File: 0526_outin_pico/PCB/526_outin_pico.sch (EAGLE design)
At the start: 16 parts

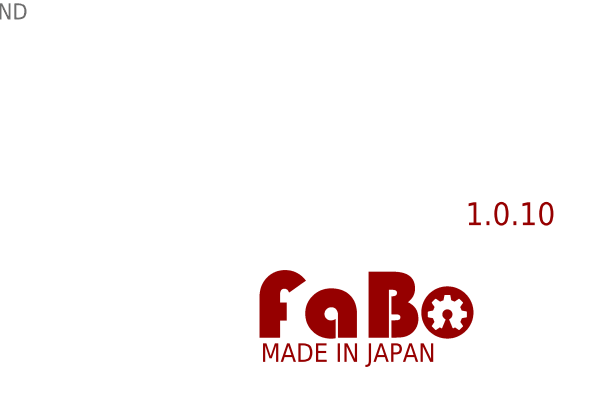
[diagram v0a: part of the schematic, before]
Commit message: #526 outin_pico　ロゴ修正
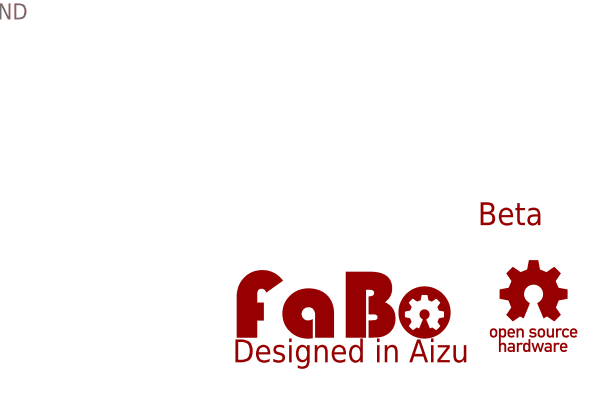
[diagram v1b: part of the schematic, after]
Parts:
- removed U$10: (no value), FaBo-etc:LOGO_FABO-M
- added LOGO1: (no value), component:LOGO_FABO-M
- added U$3: LOGO_OSHW-M_BOTTOM, component:LOGO_OSHW-M_BOTTOM
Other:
- note added: "Beta"
- note removed: "1.0.10"
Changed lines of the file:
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@@
 <?xml version="1.0" encoding="utf-8"?>
 <!DOCTYPE eagle SYSTEM "eagle.dtd">
-<eagle version="9.5.1">
+<eagle version="9.6.2">
 <drawing>
 <settings>
@@
 <setting verticaltext="up"/>
 </settings>
-<grid distance="0.1" unitdist="inch" unit="inch" style="lines" multiple="1" display="no" altdistance="0.01" altunitdist="inch" altunit="inch"/>
+<grid distance="0.1" unitdist="inch" unit="inch" style="lines" multiple="1" display="yes" altdistance="0.01" altunitdist="inch" altunit="inch"/>
 <layers>
 <layer number="1" name="Top" color="4" fill="1" visible="no" active="no"/>
@@
 </classes>
 <parts>
-<part name="U$10" library="FaBo-etc" deviceset="LOGO_FABO" device="-M"/>
 <part name="D3P" library="FaBo-Template" deviceset="FABO_BRICK_3PIN" device="-HEADER"/>
 <part name="D5P" library="FaBo-Template" deviceset="FABO_BRICK_3PIN" device="-HEADER"/>
@@
 <part name="D5" library="FaBo-Template" deviceset="FABO_BRICK_3PIN" device="-B03B-PASK-1"/>
 <part name="I2C_TOP1" library="FaBo-Template" deviceset="FABO_BRICK_I2C" device="-B04B-PASK-1"/>
+<part name="U$3" library="component" deviceset="LOGO_OSHW" device="-M_BOTTOM"/>
+<part name="LOGO1" library="component" deviceset="LOGO_FABO" device="-M"/>
 </parts>
 <sheets>
 <sheet>
 <plain>
-<text x="373.38" y="20.32" size="2.54" layer="94" align="bottom-center">1.0.10</text>
+<text x="373.38" y="20.32" size="2.54" layer="94" align="bottom-center">Beta</text>
 <text x="208.28" y="198.12" size="2.54" layer="97">DIGITAL (3pin Top 2mm pitch)</text>
 <text x="208.28" y="236.22" size="2.54" layer="97">ANALOG (3pin Side 2mm pitch)</text>
@@
 </plain>
 <instances>
-<instance part="U$10" gate="G$1" x="345.44" y="5.08" smashed="yes"/>
 <instance part="D3P" gate="G$1" x="218.44" y="96.52" smashed="yes" rot="R90">
 <attribute name="NAME" x="210.312" y="91.44" size="1.778" layer="95" rot="R90"/>
@@
 <attribute name="NAME" x="243.332" y="43.18" size="1.778" layer="95" rot="R90"/>
 </instance>
+<instance part="U$3" gate="G$1" x="375.92" y="12.7" smashed="yes"/>
+<instance part="LOGO1" gate="G$1" x="342.9" y="5.08" smashed="yes"/>
 </instances>
 <busses>

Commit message: Pico対応ボード
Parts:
- removed U$16: (no value), RaspberryPi_Pico:RPI_PICO-TH
- added D6P1: (no value), FaBo-Template:FABO_BRICK_3PIN-HEADER
- added U$4: (no value), RaspberryPi_Pico:RPI_PICO-SMD
- renumbered A0 to ADC0, A1 to ADC1, A2 to ADC2, D2 to 2, D3 to 3, D4 to 4, D5 to 5
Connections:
- removed net N$1: U$16.AGND
- new net 5V: 2.VCC, 3.VCC, 4.VCC, 5.VCC, ADC0.VCC, ADC1.VCC, ADC2.VCC, D3P.VCC, D5P.VCC, D6P.VCC, D6P1.VCC, I2C_TOP.VCC, I2C_TOP1.VCC, SERIAL_HW.VCC, U$4.ADC_VREF, U$4.VBUS
- new net PWM_14: D3P.I/O, U$4.GP14
- new net PWM_15: D5P.I/O, U$4.GP15
- new net PWM_16: D6P.I/O, U$4.GP16
- new net PWM_17: D6P1.I/O, U$4.GP17
- net 3V3: now also U$4.3V3; no longer 2.VCC, 3.VCC, 4.VCC, 5.VCC, ADC0.VCC, ADC1.VCC, ADC2.VCC, D3P.VCC, D5P.VCC, D6P.VCC, I2C_TOP.VCC, I2C_TOP1.VCC, SERIAL_HW.VCC, U$16.3V3, U$16.3V3_EN, U$16.ADC_VREF
- net A0: now also U$4.GP26_A0; no longer D3P.I/O, U$16.GP26_A0
- net A1: now also U$4.GP27_A1; no longer D5P.I/O, U$16.GP27_A1
- net A2: now also U$4.GP28_A2; no longer D6P.I/O, U$16.GP28_A2
- net D0: now also U$4.GP0; no longer U$16.GP0
- net D1: now also U$4.GP1; no longer U$16.GP1
- net D2: now also U$4.GP2; no longer U$16.GP2
- net D3: now also U$4.GP3; no longer U$16.GP3
- net D4: now also U$4.GP4; no longer U$16.GP4
- net D5: now also U$4.GP5; no longer U$16.GP5
- net GND: now also D6P1.GND, U$4.AGND, U$4.GND; no longer U$16.GND
- net RESET: now also U$4.RUN; no longer U$16.RUN
- net SCL: now also U$4.GP9; no longer U$16.GP9
- net SDA: now also U$4.GP8; no longer U$16.GP8

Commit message: OUT/IN for Raspberry Pi Pico(Rev.Beta1)　追加
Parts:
- removed 2, 3, 4, 5: (no value), FaBo-Template:FABO_BRICK_3PIN-B03B-PASK-1
- removed ADC0, ADC1, ADC2: (no value), FaBo-Template:FABO_BRICK_3PIN-S03B-PASK-2_LONG
- removed D3P, D5P, D6P, D6P1: (no value), FaBo-Template:FABO_BRICK_3PIN-HEADER
- removed I2C_TOP, I2C_TOP1: (no value), FaBo-Template:FABO_BRICK_I2C-B04B-PASK-1
- removed SERIAL_HW: (no value), FaBo-Template:FABO_BRICK_SERIAL-B04B-PASK-1
- removed U$3: LOGO_OSHW-M_BOTTOM, component:LOGO_OSHW-M_BOTTOM
- removed U$4: (no value), RaspberryPi_Pico:RPI_PICO-SMD
- added A0, A1, A2: (no value), FaBo-Template:FABO_BRICK_3PIN-S03B-PASK-2_LONG
- added D2, D3, D4, D5: (no value), FaBo-Template:FABO_BRICK_3PIN-B03B-PASK-1
- added I2C0, I2C1: (no value), FaBo-Template:FABO_BRICK_I2C-B04B-PASK-1
- added JP1: (no value), FaBo-PIN:SMD-JUMPER-2_SHORT
- added LOGO2: (no value), FaBo-Logo:LOGO_FABO-M
- added PWM14, PWM15, PWM16, PWM17: (no value), FaBo-Template:FABO_BRICK_3PIN-HEADER
- added R1, R2: 5K1, FaBo-Resistors:RESISTOR-0603
- added SERIAL: (no value), FaBo-Template:FABO_BRICK_SERIAL-B04B-PASK-1
- added U1: (no value), FaBo-Boards:RASPBERRY_PI_PICO
- LOGO1: device component:LOGO_FABO-M -> FaBo-Logo:LOGO_OSHW-M_BOTTOM
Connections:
- removed net D0: SERIAL_HW.RX, U$4.GP0
- removed net D1: SERIAL_HW.TX, U$4.GP1
- removed net PWM_14: D3P.I/O, U$4.GP14
- removed net PWM_15: D5P.I/O, U$4.GP15
- removed net PWM_16: D6P.I/O, U$4.GP16
- removed net PWM_17: D6P1.I/O, U$4.GP17
- new net AVDD: A0.VCC, A1.VCC, A2.VCC, U1.ADC_VREF
- new net N$3: JP1.2, R1.2, R2.2
- new net PWM14: PWM14.I/O, U1.GP14
- new net PWM15: PWM15.I/O, U1.GP15
- new net PWM16: PWM16.I/O, U1.GP16
- new net PWM17: PWM17.I/O, U1.GP17
- new net RX: SERIAL.RX, U1.GP1
- new net TX: SERIAL.TX, U1.GP0
- net 3V3: now also JP1.1, U1.3V3; no longer U$4.3V3
- net 5V: now also D2.VCC, D3.VCC, D4.VCC, D5.VCC, I2C0.VCC, I2C1.VCC, PWM14.VCC, PWM15.VCC, PWM16.VCC, PWM17.VCC, SERIAL.VCC, U1.VBUS; no longer 2.VCC, 3.VCC, 4.VCC, 5.VCC, ADC0.VCC, ADC1.VCC, ADC2.VCC, D3P.VCC, D5P.VCC, D6P.VCC, D6P1.VCC, I2C_TOP.VCC, I2C_TOP1.VCC, SERIAL_HW.VCC, U$4.ADC_VREF, U$4.VBUS
- net A0: now also A0.I/O, U1.GP26; no longer ADC0.I/O, U$4.GP26_A0
- net A1: now also A1.I/O, U1.GP27; no longer ADC1.I/O, U$4.GP27_A1
- net A2: now also A2.I/O, U1.GP28; no longer ADC2.I/O, U$4.GP28_A2
- net D2: now also D2.I/O, U1.GP2; no longer 2.I/O, U$4.GP2
- net D3: now also D3.I/O, U1.GP3; no longer 3.I/O, U$4.GP3
- net D4: now also D4.I/O, U1.GP4; no longer 4.I/O, U$4.GP4
- net D5: now also D5.I/O, U1.GP5; no longer 5.I/O, U$4.GP5
- net GND: now also A0.GND, A1.GND, A2.GND, D2.GND, D3.GND, D4.GND, D5.GND, I2C0.GND, I2C1.GND, PWM14.GND, PWM15.GND, PWM16.GND, PWM17.GND, S1.4, SERIAL.GND, U1.AGND@33, U1.GND@13, U1.GND@18, U1.GND@23, U1.GND@28, U1.GND@3, U1.GND@38, U1.GND@8, U1.GND@D2; no longer 2.GND, 3.GND, 4.GND, 5.GND, ADC0.GND, ADC1.GND, ADC2.GND, D3P.GND, D5P.GND, D6P.GND, D6P1.GND, I2C_TOP.GND, I2C_TOP1.GND, SERIAL_HW.GND, U$4.AGND, U$4.GND
- net RESET: now also S1.1, U1.RUN; no longer U$4.RUN
- net SCL: now also I2C0.SCL, I2C1.SCL, R1.1, U1.GP9; no longer I2C_TOP.SCL, I2C_TOP1.SCL, U$4.GP9
- net SDA: now also I2C0.SDA, I2C1.SDA, R2.1, U1.GP8; no longer I2C_TOP.SDA, I2C_TOP1.SDA, U$4.GP8
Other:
- note added: "Beta1"
- note added: "I2C Pull Up"
- note added: "Serial (4pin 2mm pitch)"
- note removed: "Beta"
- note removed: "Serial (4pin 2mm pitch) Hard/Soft"
- moved on the sheet: S1

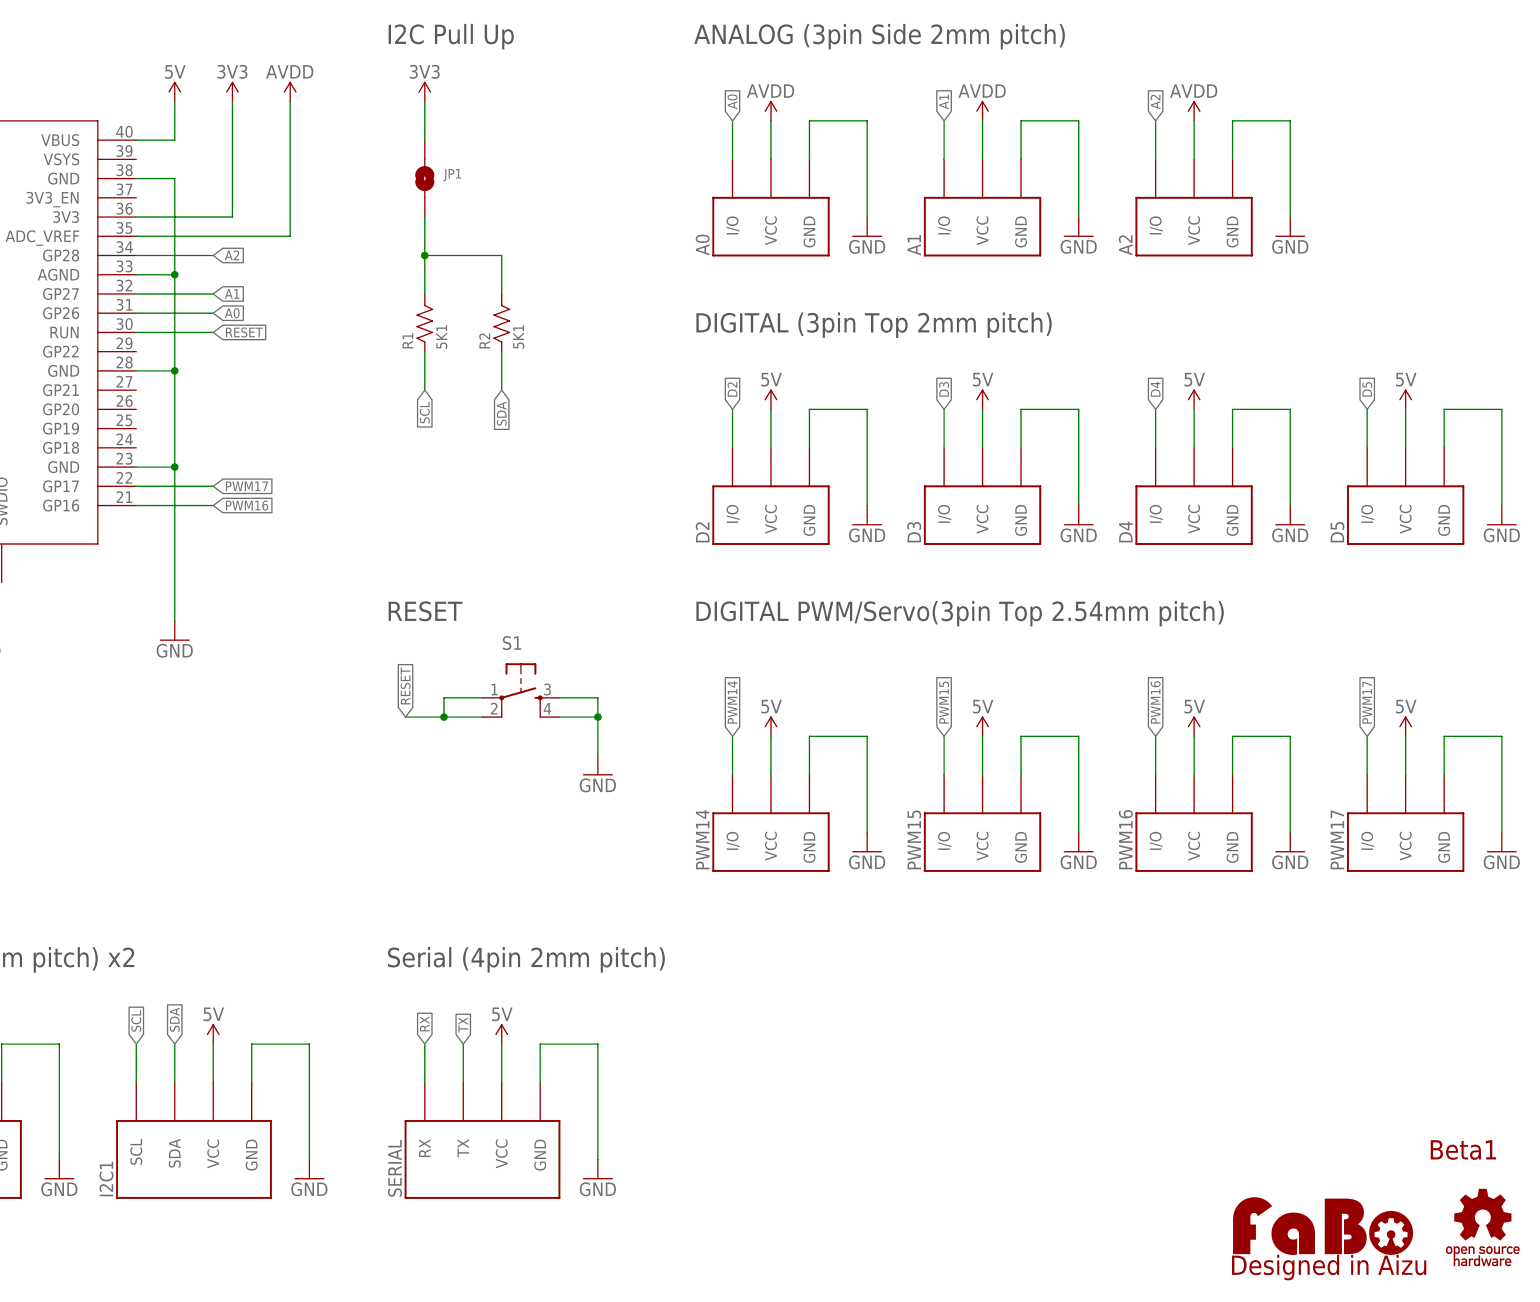
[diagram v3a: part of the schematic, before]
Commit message: アナログ用電源ピンを変更
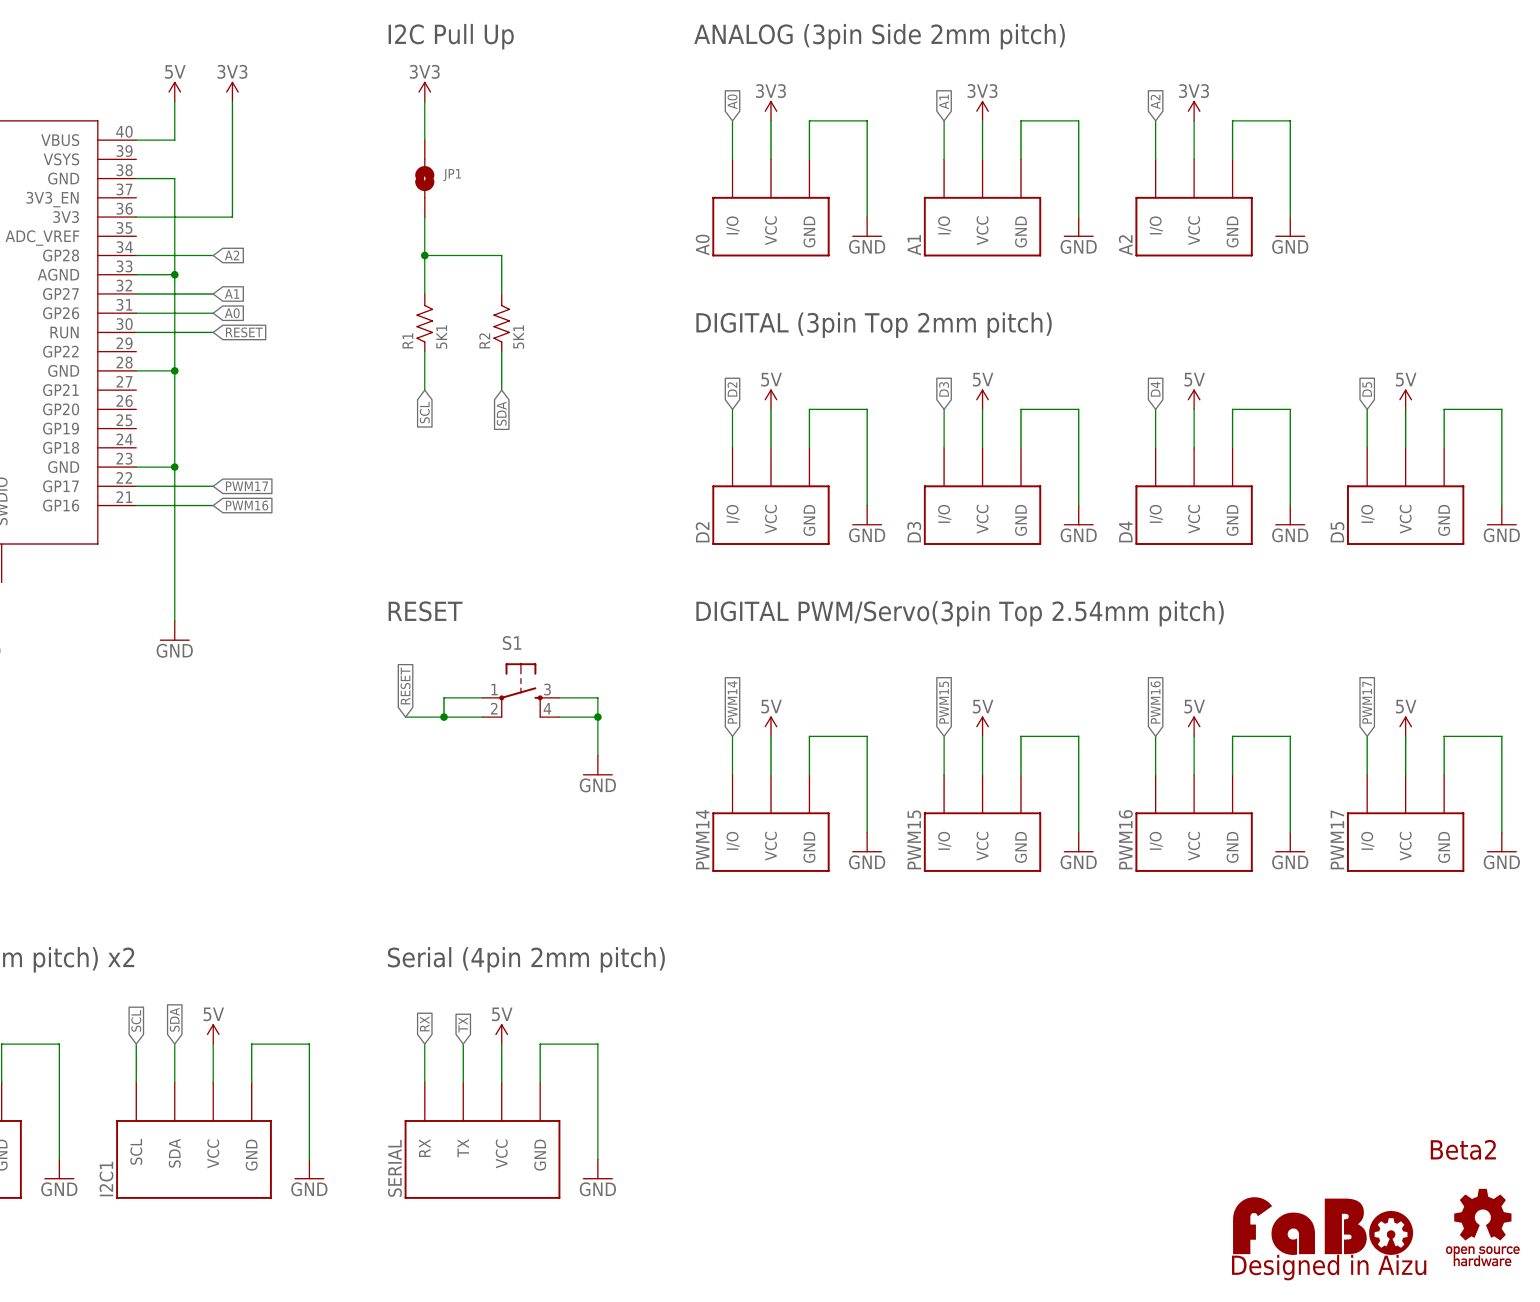
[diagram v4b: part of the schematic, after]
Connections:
- removed net AVDD: A0.VCC, A1.VCC, A2.VCC, U1.ADC_VREF
- net 3V3: now also A0.VCC, A1.VCC, A2.VCC
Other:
- note added: "Beta2"
- note removed: "Beta1"
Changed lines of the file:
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@@
 <part name="U1" library="FaBo-Boards" deviceset="RASPBERRY_PI_PICO" device=""/>
 <part name="5V1" library="FaBo-Symbol" deviceset="5V" device=""/>
-<part name="AVDD1" library="FaBo-Symbol" deviceset="AVDD" device=""/>
 <part name="GND8" library="FaBo-Symbol" deviceset="GND" device=""/>
 <part name="GND9" library="FaBo-Symbol" deviceset="GND" device=""/>
 <part name="GND14" library="FaBo-Symbol" deviceset="GND" device=""/>
-<part name="AVDD2" library="FaBo-Symbol" deviceset="AVDD" device=""/>
-<part name="AVDD3" library="FaBo-Symbol" deviceset="AVDD" device=""/>
-<part name="AVDD4" library="FaBo-Symbol" deviceset="AVDD" device=""/>
 <part name="GND1" library="FaBo-Symbol" deviceset="GND" device=""/>
 <part name="GND2" library="FaBo-Symbol" deviceset="GND" device=""/>
@@
 <part name="3V1" library="FaBo-Symbol" deviceset="3V3" device=""/>
 <part name="3V2" library="FaBo-Symbol" deviceset="3V3" device=""/>
+<part name="3V3" library="FaBo-Symbol" deviceset="3V3" device=""/>
+<part name="3V4" library="FaBo-Symbol" deviceset="3V3" device=""/>
+<part name="3V5" library="FaBo-Symbol" deviceset="3V3" device=""/>
 </parts>
 <sheets>
 <sheet>
 <plain>
-<text x="246.38" y="20.32" size="2.54" layer="94" align="bottom-center">Beta1</text>
+<text x="246.38" y="20.32" size="2.54" layer="94" align="bottom-center">Beta2</text>
 <text x="144.78" y="129.54" size="2.54" layer="97">DIGITAL (3pin Top 2mm pitch)</text>
 <text x="144.78" y="167.64" size="2.54" layer="97">ANALOG (3pin Side 2mm pitch)</text>
@@
 <attribute name="VALUE" x="76.2" y="163.068" size="1.778" layer="96" align="bottom-center"/>
 </instance>
-<instance part="AVDD1" gate="G$1" x="91.44" y="160.02" smashed="yes">
-<attribute name="VALUE" x="91.44" y="163.068" size="1.778" layer="96" align="bottom-center"/>
-</instance>
 <instance part="GND8" gate="G$1" x="50.8" y="91.44" smashed="yes">
 <attribute name="VALUE" x="50.8" y="88.392" size="1.778" layer="96" align="top-center"/>
@@
 <instance part="GND14" gate="G$1" x="76.2" y="91.44" smashed="yes">
 <attribute name="VALUE" x="76.2" y="88.392" size="1.778" layer="96" align="top-center"/>
-</instance>
-<instance part="AVDD2" gate="G$1" x="154.94" y="157.48" smashed="yes">
-<attribute name="VALUE" x="154.94" y="160.528" size="1.778" layer="96" align="bottom-center"/>
-</instance>
-<instance part="AVDD3" gate="G$1" x="182.88" y="157.48" smashed="yes">
-<attribute name="VALUE" x="182.88" y="160.528" size="1.778" layer="96" align="bottom-center"/>
-</instance>
-<instance part="AVDD4" gate="G$1" x="210.82" y="157.48" smashed="yes">
-<attribute name="VALUE" x="210.82" y="160.528" size="1.778" layer="96" align="bottom-center"/>
 </instance>
 <instance part="GND1" gate="G$1" x="167.64" y="144.78" smashed="yes">
@@
 <instance part="3V2" gate="G$1" x="109.22" y="160.02" smashed="yes">
 <attribute name="VALUE" x="109.22" y="163.068" size="1.778" layer="96" align="bottom-center"/>
+</instance>
+<instance part="3V3" gate="G$1" x="154.94" y="157.48" smashed="yes">
+<attribute name="VALUE" x="154.94" y="160.528" size="1.778" layer="96" align="bottom-center"/>
+</instance>
+<instance part="3V4" gate="G$1" x="182.88" y="157.48" smashed="yes">
+<attribute name="VALUE" x="182.88" y="160.528" size="1.778" layer="96" align="bottom-center"/>
+</instance>
+<instance part="3V5" gate="G$1" x="210.82" y="157.48" smashed="yes">
+<attribute name="VALUE" x="210.82" y="160.528" size="1.778" layer="96" align="bottom-center"/>
 </instance>
 </instances>
@@
 </segment>
 </net>
-<net name="AVDD" class="0">
-<segment>
-<pinref part="U1" gate="G$1" pin="ADC_VREF"/>
-<pinref part="AVDD1" gate="G$1" pin="AVDD"/>
-<wire x1="71.12" y1="142.24" x2="91.44" y2="142.24" width="0.1524" layer="91"/>
-<wire x1="91.44" y1="142.24" x2="91.44" y2="160.02" width="0.1524" layer="91"/>
-</segment>
-<segment>
-<pinref part="A2" gate="G$1" pin="VCC"/>
-<pinref part="AVDD4" gate="G$1" pin="AVDD"/>
-<wire x1="210.82" y1="152.4" x2="210.82" y2="157.48" width="0.1524" layer="91"/>
-</segment>
-<segment>
-<pinref part="A1" gate="G$1" pin="VCC"/>
-<pinref part="AVDD3" gate="G$1" pin="AVDD"/>
-<wire x1="182.88" y1="152.4" x2="182.88" y2="157.48" width="0.1524" layer="91"/>
-</segment>
-<segment>
-<pinref part="AVDD2" gate="G$1" pin="AVDD"/>
-<pinref part="A0" gate="G$1" pin="VCC"/>
-<wire x1="154.94" y1="157.48" x2="154.94" y2="152.4" width="0.1524" layer="91"/>
-</segment>
-</net>
 <net name="PWM17" class="0">
 <segment>
@@
 <wire x1="109.22" y1="154.94" x2="109.22" y2="160.02" width="0.1524" layer="91"/>
 </segment>
-</net>
+<segment>
+<pinref part="A2" gate="G$1" pin="VCC"/>
+<pinref part="3V5" gate="G$1" pin="3V3"/>
+<wire x1="210.82" y1="152.4" x2="210.82" y2="157.48" width="0.1524" layer="91"/>
+</segment>
+<segment>
+<pinref part="A1" gate="G$1" pin="VCC"/>
+<pinref part="3V4" gate="G$1" pin="3V3"/>
+<wire x1="182.88" y1="152.4" x2="182.88" y2="157.48" width="0.1524" layer="91"/>
+</segment>
+<segment>
+<pinref part="A0" gate="G$1" pin="VCC"/>
+<pinref part="3V3" gate="G$1" pin="3V3"/>
+<wire x1="154.94" y1="152.4" x2="154.94" y2="157.48" width="0.1524" layer="91"/>
+</segment>
+</net>
